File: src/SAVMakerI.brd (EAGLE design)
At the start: 53.3 x 53.3 mm, 48 parts, among them J2 AVR_SPI_PRG_6PTH, U1 ATMEGA32U4-AU, Y1 RESONATORSMD

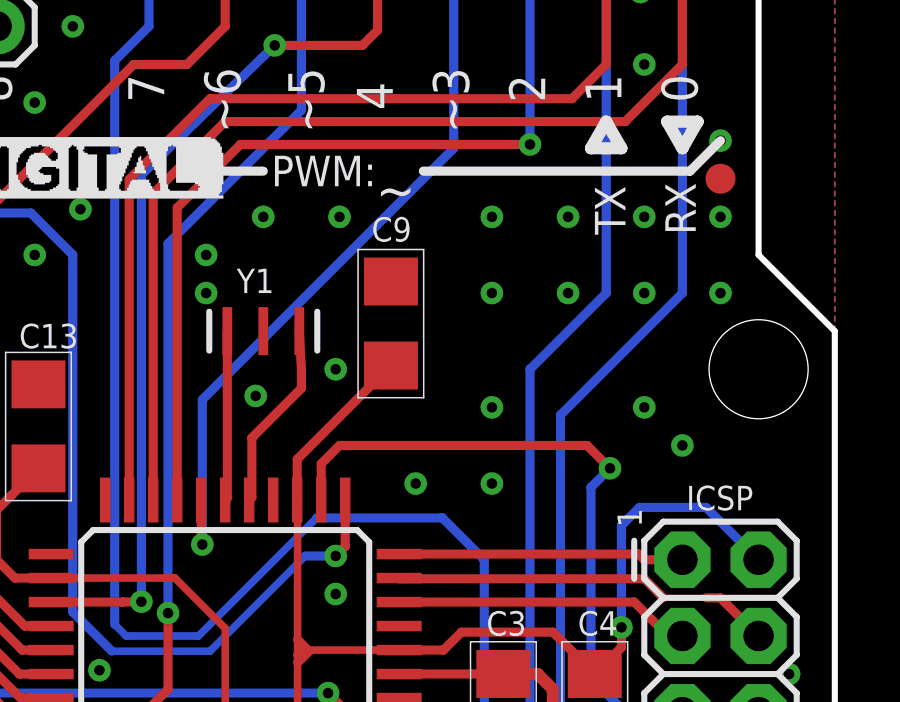
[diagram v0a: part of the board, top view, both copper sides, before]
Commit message: Added oscillator replacing the resonator.
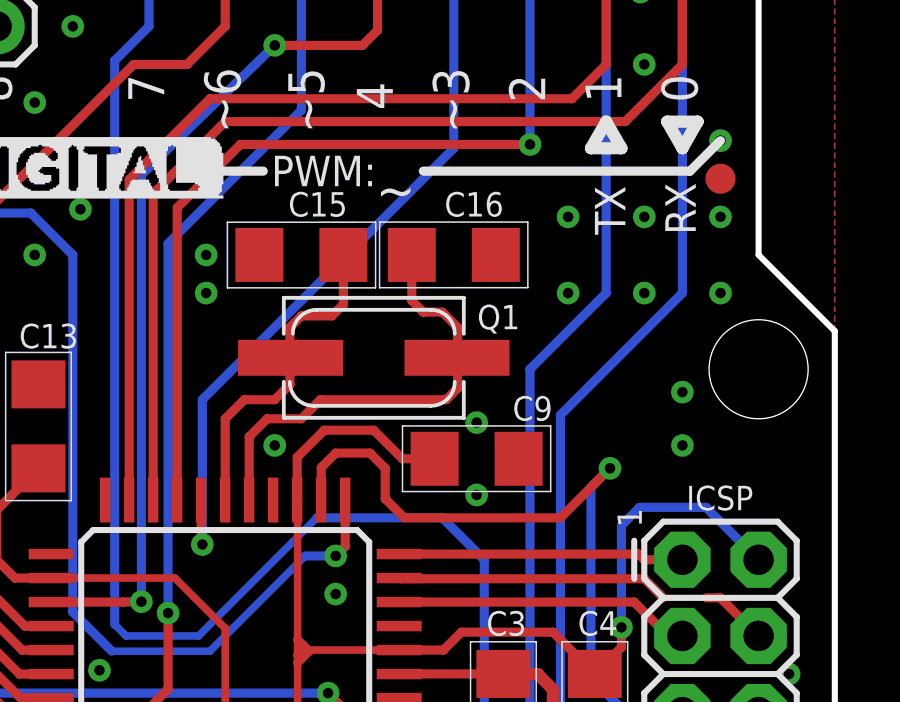
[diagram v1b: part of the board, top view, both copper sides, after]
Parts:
- removed Y1: RESONATORSMD, sparkfun_2:RESONATOR-SMD
- added C15, C16: 18pF, sparkfun_2:1206
- added Q1: CSM-3X-CRYSTALCSM-3X, fmc:CSM-3X
- moved C9 5.34 mm to (41.4, 33.8), turned to 0 degrees
- renumbered A to B
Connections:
- net GND: now also C15.2, C16.2; no longer Y1.2
- net N$3: now also C16.1, Q1.2; no longer Y1.3
- net N$4: now also C15.1, Q1.1; no longer Y1.1
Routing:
- net N$3: track 6.35 -> 15.2 mm
- net N$4: track 5.66 -> 11.0 mm
- net RESET: track 76.4 -> 78.1 mm
- net VCC: track 125.2 -> 126.2 mm
- net GND: vias 125 -> 119

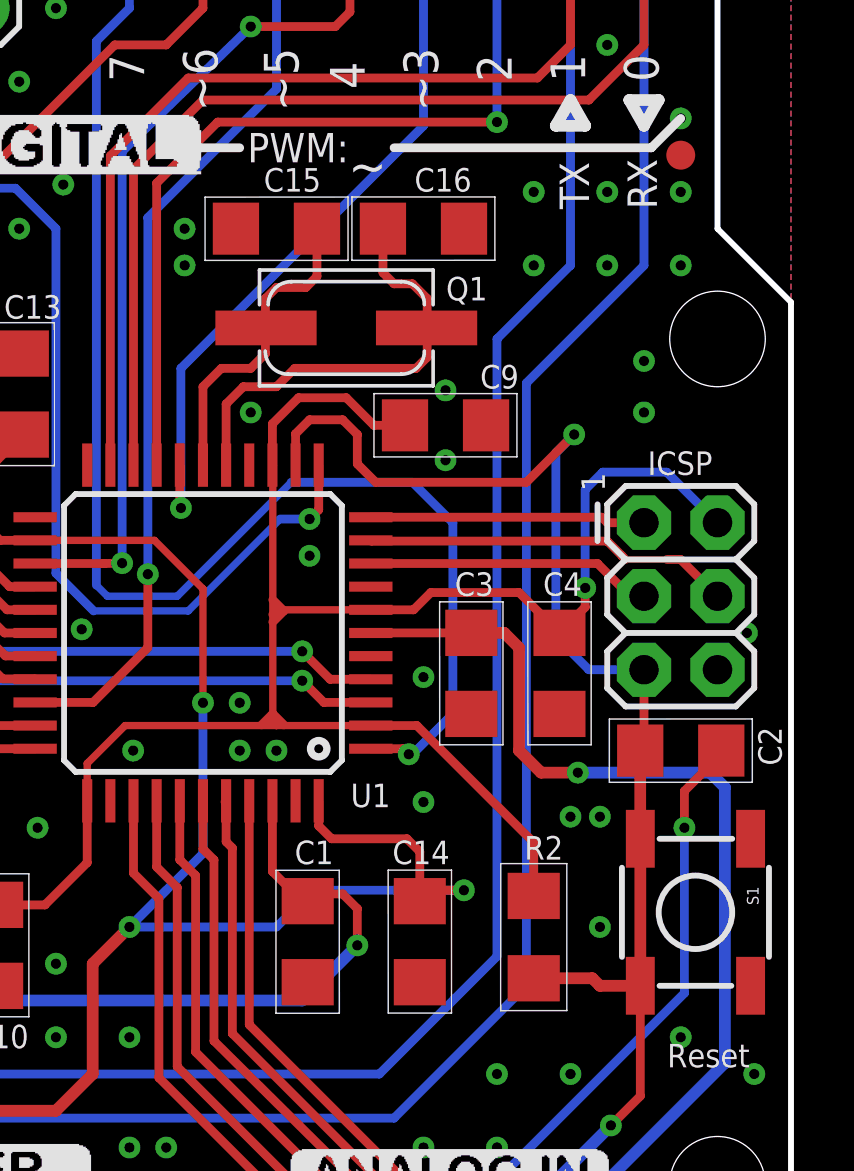
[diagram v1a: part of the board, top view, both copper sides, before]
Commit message: Minor modifications to routes.
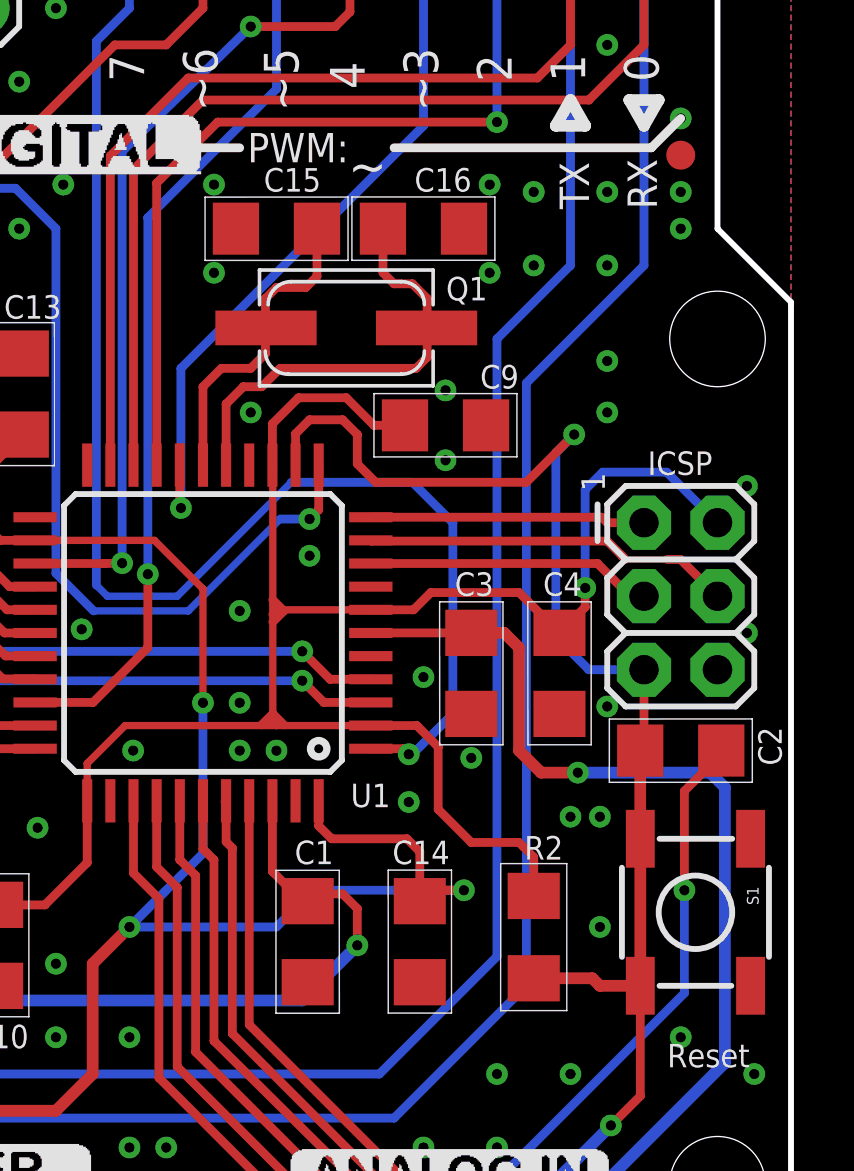
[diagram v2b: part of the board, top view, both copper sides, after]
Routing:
- net VCC: track 126.2 -> 127.1 mm
- net GND: vias 119 -> 125
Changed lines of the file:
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@@
 <wire x1="46.228" y1="27.562" x2="46.228" y2="28.2258" width="0.3048" layer="1"/>
 <wire x1="45.339" y1="26.673" x2="46.228" y2="27.562" width="0.3048" layer="1"/>
-<wire x1="44.45" y1="19.431" x2="44.45" y2="17.5828" width="0.3048" layer="1"/>
-<wire x1="40.411" y1="23.47" x2="44.45" y2="19.431" width="0.3048" layer="1"/>
 <wire x1="46.228" y1="28.2258" x2="46.228" y2="31.623" width="0.3048" layer="16"/>
 <wire x1="46.228" y1="31.623" x2="46.8313" y2="32.2263" width="0.3048" layer="16"/>
@@
 <wire x1="37.973" y1="34.798" x2="38.9255" y2="33.8455" width="0.3048" layer="1"/>
 <wire x1="40.002" y1="33.8455" x2="38.9255" y2="33.8455" width="0.3048" layer="1"/>
+<wire x1="40.411" y1="23.47" x2="41.148" y2="22.733" width="0.3048" layer="1"/>
+<wire x1="41.148" y1="22.733" x2="41.148" y2="20.574" width="0.3048" layer="1"/>
+<wire x1="41.148" y1="20.574" x2="42.291" y2="19.431" width="0.3048" layer="1"/>
+<wire x1="42.291" y1="19.431" x2="43.942" y2="19.431" width="0.3048" layer="1"/>
+<wire x1="43.942" y1="19.431" x2="44.45" y2="18.923" width="0.3048" layer="1"/>
+<wire x1="44.45" y1="18.923" x2="44.45" y2="17.5828" width="0.3048" layer="1"/>
 <wire x1="50.8" y1="30.4737" x2="50.8" y2="30.48" width="0" layer="19" extent="16-16"/>
 </signal>
@@
 <wire x1="40.767" y1="38.227" x2="40.767" y2="37.23" width="0.3048" layer="1"/>
 <wire x1="40.767" y1="37.23" x2="40.748" y2="37.211" width="0.3048" layer="1"/>
-<wire x1="36.195" y1="35.814" x2="40.386" y2="35.814" width="0.3048" layer="1"/>
+<wire x1="35.687" y1="35.814" x2="40.386" y2="35.814" width="0.3048" layer="1"/>
 <wire x1="40.386" y1="35.814" x2="40.767" y2="36.195" width="0.3048" layer="1"/>
 <wire x1="40.767" y1="36.195" x2="40.767" y2="37.192" width="0.3048" layer="1"/>
@@
 <wire x1="33.82" y1="32.47" x2="33.82" y2="34.582" width="0.3048" layer="1"/>
 <wire x1="33.82" y1="34.582" x2="34.417" y2="35.179" width="0.3048" layer="1"/>
-<wire x1="34.417" y1="35.179" x2="35.56" y2="35.179" width="0.3048" layer="1"/>
-<wire x1="35.56" y1="35.179" x2="36.195" y2="35.814" width="0.3048" layer="1"/>
+<wire x1="34.417" y1="35.179" x2="35.052" y2="35.179" width="0.3048" layer="1"/>
+<wire x1="35.052" y1="35.179" x2="35.687" y2="35.814" width="0.3048" layer="1"/>
 </signal>
 <signal name="N$4">
@@
 <via x="43.18" y="8.89" extent="1-16" drill="0.35"/>
 <via x="46.99" y="39.37" extent="1-16" drill="0.35"/>
-<via x="49.53" y="39.37" extent="1-16" drill="0.35"/>
+<via x="49.53" y="40.64" extent="1-16" drill="0.35"/>
 <via x="34.29" y="49.53" extent="1-16" drill="0.35"/>
 <via x="46.99" y="46.99" extent="1-16" drill="0.35"/>
@@
 <via x="31.75" y="8.89" extent="1-16" drill="0.35"/>
 <via x="30.48" y="8.89" extent="1-16" drill="0.35"/>
-<via x="40.64" y="20.828" extent="1-16" drill="0.35"/>
+<via x="40.132" y="20.828" extent="1-16" drill="0.35"/>
 <via x="10.16" y="5.08" extent="1-16" drill="0.35"/>
 <via x="10.16" y="2.54" extent="1-16" drill="0.35"/>
@@
 <via x="44.45" y="41.91" extent="1-16" drill="0.35"/>
 <via x="44.45" y="39.37" extent="1-16" drill="0.35"/>
-<via x="32.385" y="39.37" extent="1-16" drill="0.35"/>
-<via x="32.385" y="40.64" extent="1-16" drill="0.35"/>
+<via x="33.401" y="39.116" extent="1-16" drill="0.35"/>
+<via x="33.401" y="42.164" extent="1-16" drill="0.35"/>
 <via x="41.402" y="35.052" extent="1-16" drill="0.35"/>
 <contactref element="JP1" pad="7"/>
@@
 <via x="10.16" y="26.67" extent="1-16" drill="0.35"/>
 <via x="2.54" y="25.4" extent="1-16" drill="0.35"/>
-<via x="48.26" y="36.068" extent="1-16" drill="0.35"/>
+<via x="46.99" y="36.068" extent="1-16" drill="0.35"/>
 <via x="6.35" y="17.78" extent="1-16" drill="0.35"/>
 <via x="10.16" y="17.78" extent="1-16" drill="0.35"/>
@@
 <via x="28.829" y="26.797" extent="1-16" drill="0.35"/>
 <via x="52.07" y="11.43" extent="1-16" drill="0.35"/>
-<via x="48.26" y="34.29" extent="1-16" drill="0.35"/>
+<via x="46.99" y="34.29" extent="1-16" drill="0.35"/>
 <via x="34.671" y="34.29" extent="1-16" drill="0.35"/>
 <via x="49.53" y="12.7" extent="1-16" drill="0.35"/>
@@
 <contactref element="C16" pad="2"/>
 <via x="41.402" y="32.639" extent="1-16" drill="0.35"/>
+<via x="34.29" y="27.432" extent="1-16" drill="0.35"/>
+<via x="42.926" y="42.164" extent="1-16" drill="0.35"/>
+<via x="42.926" y="39.116" extent="1-16" drill="0.35"/>
+<via x="51.816" y="31.75" extent="1-16" drill="0.35"/>
+<via x="46.99" y="24.13" extent="1-16" drill="0.35"/>
+<via x="42.291" y="22.352" extent="1-16" drill="0.35"/>
 </signal>
 <signal name="TXLED">
@@
 <wire x1="50.93" y1="22.606" x2="50.93" y2="22.482" width="0.3048" layer="1"/>
 <wire x1="50.93" y1="22.482" x2="49.657" y2="21.209" width="0.3048" layer="1"/>
-<wire x1="49.657" y1="21.209" x2="49.657" y2="19.939" width="0.3048" layer="1"/>
-<via x="49.657" y="19.939" extent="1-16" drill="0.35"/>
-<wire x1="49.657" y1="19.939" x2="49.657" y2="14.224" width="0.3048" layer="16"/>
+<wire x1="49.657" y1="21.209" x2="49.657" y2="17.78" width="0.3048" layer="1"/>
+<via x="49.657" y="17.78" extent="1-16" drill="0.35"/>
+<wire x1="49.657" y1="17.78" x2="49.657" y2="14.224" width="0.3048" layer="16"/>
 </signal>
 <signal name="VIN" class="1">

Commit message: Updated routing.
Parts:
- moved U$13 15.1 mm to (9.91, 1.40)
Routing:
- net AVCC: track 63.1 -> 61.1 mm
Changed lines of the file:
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@@
 <layer number="14" name="Route14" color="1" fill="6" visible="no" active="no"/>
 <layer number="15" name="Route15" color="4" fill="6" visible="no" active="no"/>
-<layer number="16" name="Bottom" color="1" fill="1" visible="yes" active="yes"/>
+<layer number="16" name="Bottom" color="1" fill="1" visible="no" active="yes"/>
 <layer number="17" name="Pads" color="2" fill="1" visible="yes" active="yes"/>
 <layer number="18" name="Vias" color="2" fill="1" visible="yes" active="yes"/>
@@
 <layer number="37" name="tTest" color="7" fill="1" visible="no" active="yes"/>
 <layer number="38" name="bTest" color="7" fill="1" visible="no" active="yes"/>
-<layer number="39" name="tKeepout" color="4" fill="11" visible="yes" active="yes"/>
+<layer number="39" name="tKeepout" color="4" fill="11" visible="no" active="yes"/>
 <layer number="40" name="bKeepout" color="1" fill="11" visible="no" active="yes"/>
-<layer number="41" name="tRestrict" color="4" fill="10" visible="yes" active="yes"/>
+<layer number="41" name="tRestrict" color="4" fill="10" visible="no" active="yes"/>
 <layer number="42" name="bRestrict" color="1" fill="10" visible="no" active="yes"/>
 <layer number="43" name="vRestrict" color="2" fill="10" visible="no" active="yes"/>
@@
 <layer number="45" name="Holes" color="7" fill="1" visible="no" active="yes"/>
 <layer number="46" name="Milling" color="3" fill="1" visible="no" active="yes"/>
-<layer number="47" name="Measures" color="7" fill="1" visible="yes" active="yes"/>
+<layer number="47" name="Measures" color="7" fill="1" visible="no" active="yes"/>
 <layer number="48" name="Document" color="7" fill="1" visible="no" active="yes"/>
 <layer number="49" name="Reference" color="7" fill="1" visible="no" active="yes"/>
@@
 <vertex x="40.767" y="22.225"/>
 </polygon>
-<dimension x1="49.00395" y1="53.34" x2="49.53" y2="0" x3="60.6958625" y3="26.782715625" textsize="1.778" layer="47"/>
-<dimension x1="0" y1="49.7479" x2="53.34" y2="49.53" x3="26.701125" y3="57.258821875" textsize="1.778" layer="47"/>
+<dimension x1="0" y1="0" x2="0" y2="53.34" x3="64.77" y3="26.67" textsize="1" layer="47" dtype="horizontal"/>
+<dimension x1="0" y1="53.34" x2="53.34" y2="53.34" x3="26.67" y3="59.69" textsize="1" layer="47" dtype="horizontal"/>
 </plain>
 <attributes>
@@
 <elements>
 <element name="C10" library="sparkfun_2" package="1206" value="0.1uF" x="25.908" y="15.875" smashed="yes" rot="R270">
-<attribute name="NAME" x="25.019" y="12.319" size="0.8128" layer="21" font="vector" ratio="10"/>
+<attribute name="NAME" x="24.892" y="18.542" size="0.8128" layer="21" font="vector" ratio="10"/>
 </element>
 <element name="R11" library="adafruit" package="R1206" value="2K2" x="18.034" y="28.956" smashed="yes">
@@
 </element>
 <element name="L1" library="wuerth-elektronik" package="1206W" value="Ferrite" x="23.114" y="15.875" smashed="yes" rot="R270">
-<attribute name="NAME" x="22.544" y="12.3825" size="0.8128" layer="21" font="vector" ratio="10"/>
+<attribute name="NAME" x="22.544" y="18.6055" size="0.8128" layer="21" font="vector" ratio="10"/>
 </element>
 <element name="C12" library="sparkfun_2" package="1206" value="1uF" x="20.193" y="15.8115" smashed="yes" rot="R270">
-<attribute name="NAME" x="19.2459" y="12.2668" size="0.8128" layer="21" font="vector" ratio="10"/>
+<attribute name="NAME" x="19.1189" y="18.4898" size="0.8128" layer="21" font="vector" ratio="10"/>
 </element>
 <element name="C14" library="sparkfun_2" package="1206" value="0.1uF" x="40.513" y="16.002" smashed="yes" rot="R270">
@@
 <element name="U$17" library="SAVMakerI" package="DIGITAL_BMP" value="" x="22.987" y="42.545"/>
 <element name="U$18" library="SAVMakerI" package="POWER_BMP" value="" x="19.177" y="7.239"/>
-<element name="U$13" library="SAVMakerI" package="OSHW" value="" x="10.16" y="16.51"/>
+<element name="U$13" library="SAVMakerI" package="OSHW" value="" x="9.906" y="1.397"/>
 <element name="B" library="fmc" package="BOARD_INFO_BMP" value="SAV Maker I" x="36.83" y="24.13" rot="MR0"/>
 <element name="U$14" library="fmc" package="CERN_OHL" value="" x="36.83" y="17.78" rot="MR0"/>
@@
 <wire x1="37.465" y1="19.558" x2="37.02" y2="20.003" width="0.3048" layer="1"/>
 <wire x1="40.0685" y1="19.558" x2="37.465" y2="19.558" width="0.3048" layer="1"/>
-<wire x1="30.48" y1="16.51" x2="33.02" y2="19.05" width="0.3048" layer="16"/>
 <wire x1="33.02" y1="19.05" x2="33.02" y2="24.257" width="0.3048" layer="16"/>
-<wire x1="30.48" y1="16.51" x2="31.75" y2="17.78" width="0.3048" layer="16"/>
 <wire x1="25.905" y1="32.636" x2="26.797" y2="33.525" width="0.3048" layer="1"/>
 <wire x1="25.4" y1="32.131" x2="25.905" y2="32.636" width="0.3048" layer="1"/>
@@
 <wire x1="36.83" y1="17.78" x2="42.037" y2="17.78" width="0.3048" layer="16"/>
 <wire x1="35.56" y1="16.51" x2="36.83" y2="17.78" width="0.3048" layer="16"/>
-<wire x1="30.48" y1="16.51" x2="35.56" y2="16.51" width="0.3048" layer="16"/>
-<wire x1="30.479" y1="16.51" x2="30.48" y2="16.51" width="0.4064" layer="1"/>
-<via x="30.48" y="16.51" extent="1-16" drill="0.35"/>
+<wire x1="29.718" y1="16.51" x2="35.56" y2="16.51" width="0.3048" layer="16"/>
+<wire x1="29.717" y1="16.51" x2="29.718" y2="16.51" width="0.4064" layer="1"/>
+<via x="29.718" y="16.51" extent="1-16" drill="0.35"/>
 <via x="42.037" y="17.78" extent="1-16" drill="0.35"/>
 <via x="33.02" y="24.257" extent="1-16" drill="0.35"/>
@@
 <wire x1="40.513" y1="17.78" x2="40.513" y2="17.402" width="0.3048" layer="1"/>
 <contactref element="C13" pad="1"/>
-<wire x1="23.114" y1="14.475" x2="23.114" y2="11.176" width="0.4064" layer="1"/>
-<wire x1="23.114" y1="11.176" x2="24.13" y2="10.16" width="0.4064" layer="1"/>
-<wire x1="24.13" y1="10.16" x2="27.94" y2="10.16" width="0.4064" layer="1"/>
-<wire x1="27.94" y1="10.16" x2="29.21" y2="11.43" width="0.4064" layer="1"/>
-<wire x1="29.21" y1="11.43" x2="29.21" y2="15.24" width="0.4064" layer="1"/>
-<wire x1="30.479" y1="16.51" x2="30.479" y2="16.509" width="0.4064" layer="1"/>
-<wire x1="30.479" y1="16.509" x2="29.21" y2="15.24" width="0.4064" layer="1"/>
+<wire x1="23.114" y1="14.475" x2="23.114" y2="12.26849375" width="0.4064" layer="1"/>
+<wire x1="23.114" y1="12.26849375" x2="24.20649375" y2="11.176" width="0.4064" layer="1"/>
+<wire x1="24.20649375" y1="11.176" x2="28.067" y2="11.176" width="0.4064" layer="1"/>
+<wire x1="28.067" y1="11.176" x2="29.21" y2="12.319" width="0.4064" layer="1"/>
+<wire x1="29.21" y1="12.319" x2="29.21" y2="15.113" width="0.4064" layer="1"/>
+<wire x1="29.717" y1="16.51" x2="29.209" y2="16.001" width="0.4064" layer="1"/>
+<wire x1="29.209" y1="16.001" x2="29.21" y2="15.113" width="0.4064" layer="1"/>
+<wire x1="29.718" y1="16.51" x2="29.718" y2="17.526" width="0.3048" layer="16"/>
+<wire x1="29.718" y1="17.526" x2="30.48" y2="18.288" width="0.3048" layer="16"/>
+<wire x1="30.48" y1="18.288" x2="32.258" y2="18.288" width="0.3048" layer="16"/>
+<wire x1="32.258" y1="18.288" x2="33.02" y2="19.05" width="0.3048" layer="16"/>
 </signal>
 <signal name="GND">
